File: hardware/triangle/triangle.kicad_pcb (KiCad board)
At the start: 4 copper layers, 100 x 86.6 mm, 71 parts, among them J1 USB_C_Receptacle_USB2.0_16P, J2 USB_C_Receptacle_USB2.0_16P, U2 EA8212HT6R

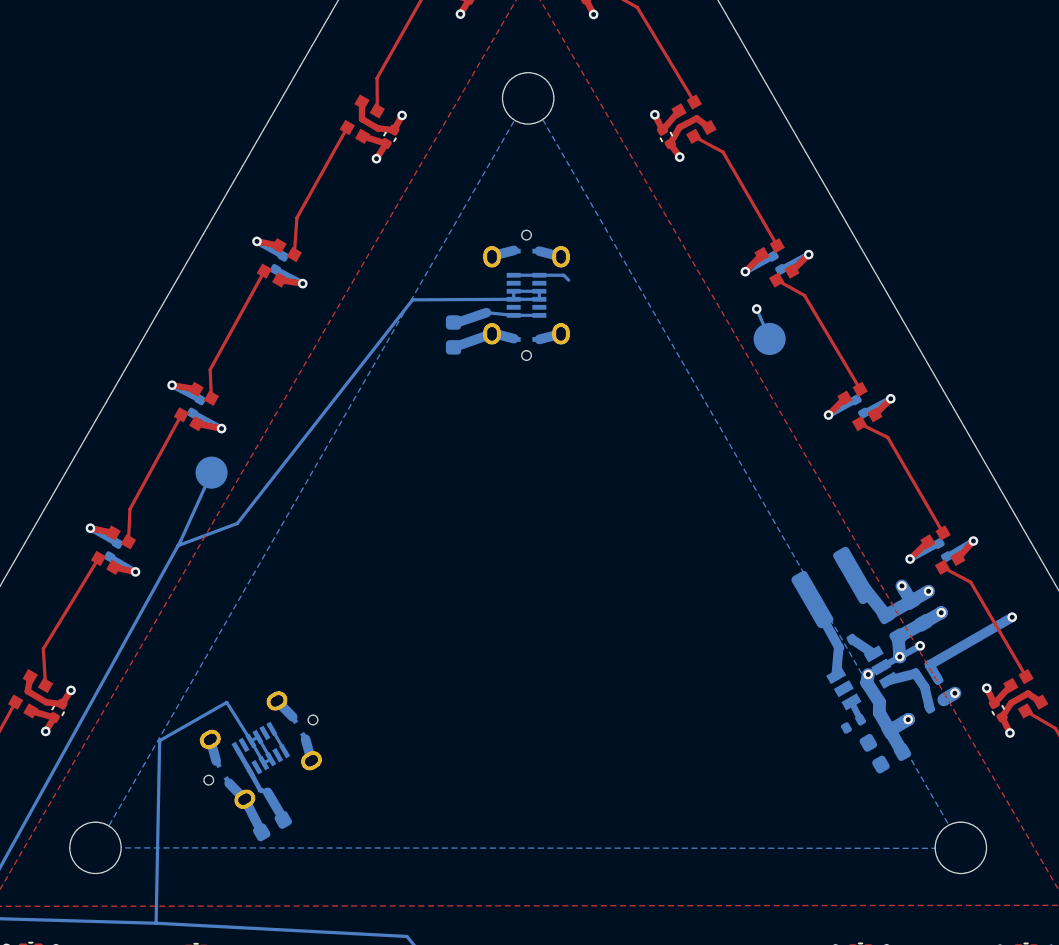
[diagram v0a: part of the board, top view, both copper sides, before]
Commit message: updates to schematic based on feedback
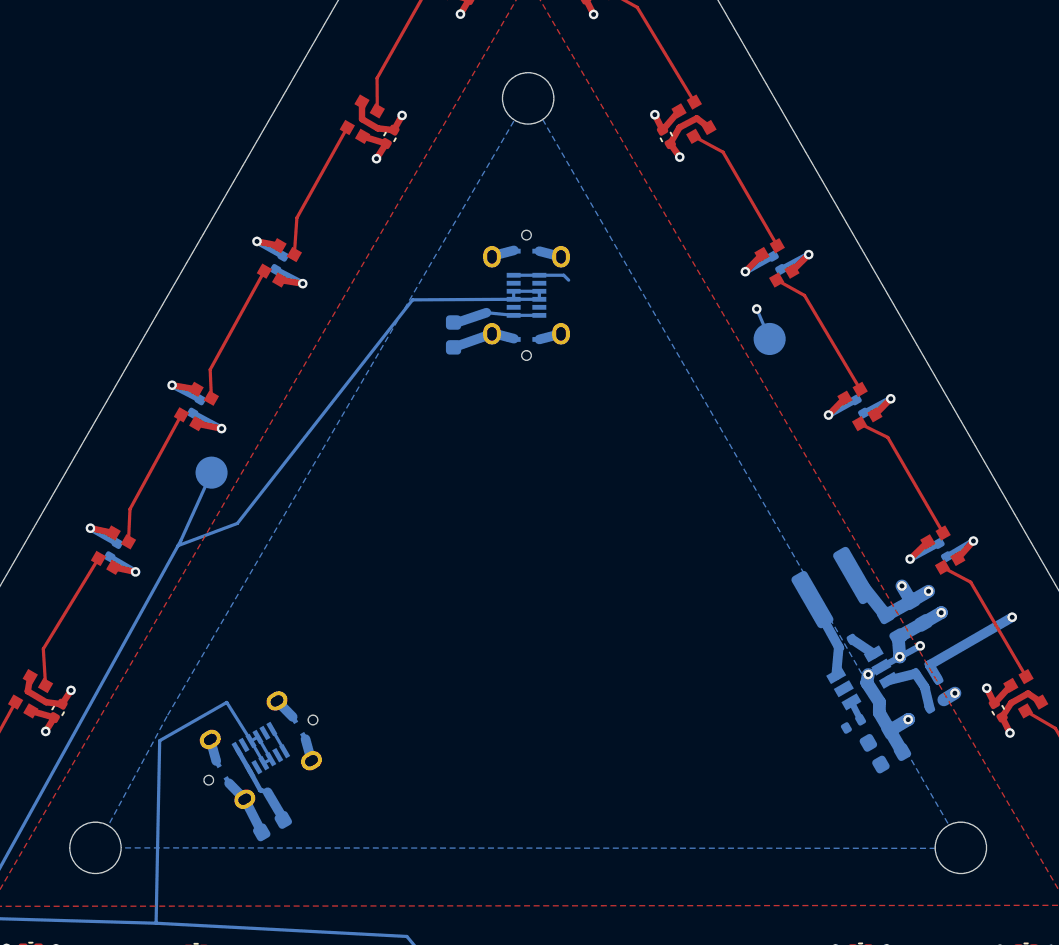
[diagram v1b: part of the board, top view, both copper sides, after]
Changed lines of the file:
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@@
 		)
 		(property "Value" "10µF"
-			(at 0 -1.430001 30)
+			(at -0.000001 -1.430001 30)
 			(layer "B.Fab")
 			(effects
@@
 		(polygon
 			(pts
-				(xy 150.01 89.87) (xy 123.09 136.7) (xy 177.05 136.73) (xy 150.02 89.78)
+				(xy 150.01 89.87) (xy 127.5 128.5) (xy 123.09 136.7) (xy 130.750025 136.704259) (xy 177.05 136.73)
+				(xy 150.02 89.78)
 			)
 		)

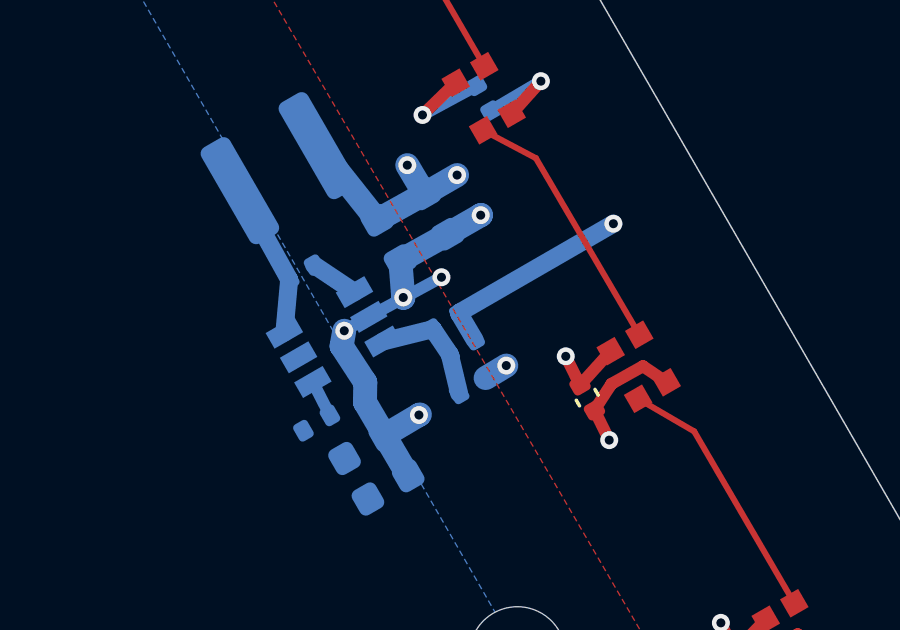
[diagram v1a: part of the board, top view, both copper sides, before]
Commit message: remove unused capacitor from triangle board
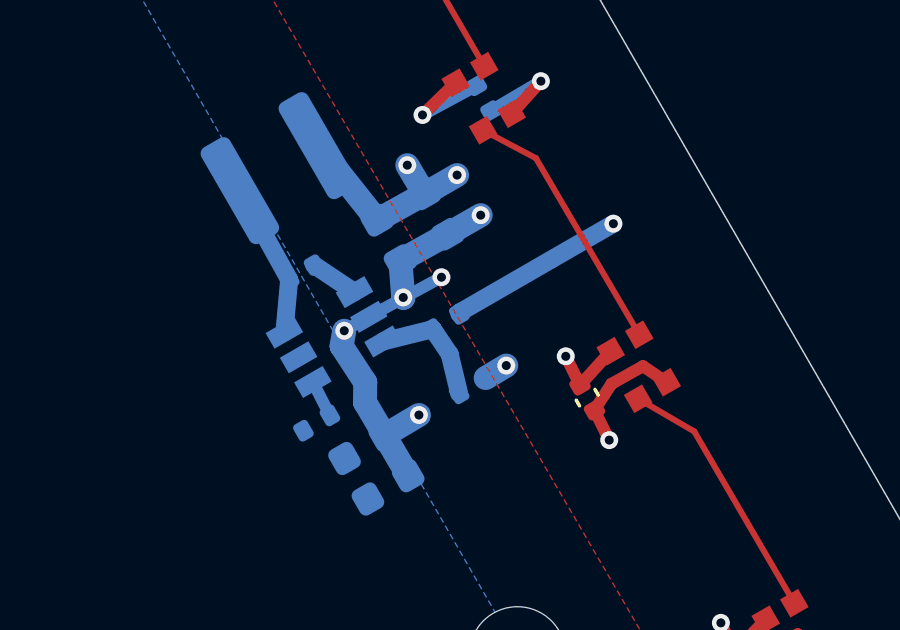
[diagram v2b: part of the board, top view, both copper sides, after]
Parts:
- removed C32: 33nF, Capacitor_SMD:C_0402_1005Metric
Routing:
- net +4V: track 112.4 -> 111.4 mm
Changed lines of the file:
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@@
 		)
 	)
-	(footprint "Capacitor_SMD:C_0402_1005Metric"
-		(layer "B.Cu")
-		(at 175.12 126.44 30)
-		(descr "Capacitor SMD 0402 (1005 Metric), square (rectangular) end terminal, IPC-7351 nominal, (Body size source: IPC-SM-782 page 76, https://www.pcb-3d.com/wordpress/wp-content/uploads/ipc-sm-782a_amendment_1_and_2.pdf)")
-		(tags "capacitor")
-		(property "Reference" "C32"
-			(at 2.606403 0.465577 210)
-			(layer "B.SilkS")
-			(effects
-				(font
-					(size 1 1)
-					(thickness 0.15)
-				)
-				(justify mirror)
-			)
-		)
-		(property "Value" "33nF"
-			(at 0 -1.16 210)
-			(layer "B.Fab")
-			(effects
-				(font
-					(size 1 1)
-					(thickness 0.15)
-				)
-				(justify mirror)
-			)
-		)
-		(property "Datasheet" "https://www.lcsc.com/datasheet/lcsc_datasheet_2304140030_Samsung-Electro-Mechanics-CL05B104KO5NNNC_C1525.pdf"
-			(at 0 0 210)
-			(layer "B.Fab")
-			(hide yes)
-			(effects
-				(font
-					(size 1.27 1.27)
-				)
-				(justify mirror)
-			)
-		)
-		(property "Description" "Unpolarized capacitor"
-			(at 0 0 210)
-			(layer "B.Fab")
-			(hide yes)
-			(effects
-				(font
-					(size 1.27 1.27)
-				)
-				(justify mirror)
-			)
-		)
-		(property "KiLib_Generator" "SMD_2terminal_chip_molded"
-			(at 0 0 210)
-			(layer "B.SilkS")
-			(hide yes)
-			(effects
-				(font
-					(size 1 1)
-					(thickness 0.15)
-				)
-				(justify mirror)
-			)
-		)
-		(property "LCSC Part #" "C507072"
-			(at 0 0 210)
-			(unlocked yes)
-			(layer "B.Fab")
-			(hide yes)
-			(effects
-				(font
-					(size 1 1)
-					(thickness 0.15)
-				)
-				(justify mirror)
-			)
-		)
-		(property ki_fp_filters "C_*")
-		(sheetname "/")
-		(sheetfile "usb_and_power.kicad_sch")
-		(units
-			(unit
-				(name "A")
-				(pins "1" "2")
-			)
-		)
-		(attr smd dnp)
-		(duplicate_pad_numbers_are_jumpers no)
-		(fp_line
-			(start -0.107836 -0.36)
-			(end 0.107836 -0.36)
-			(stroke
-				(width 0.12)
-				(type solid)
-			)
-			(layer "B.SilkS")
-		)
-		(fp_line
-			(start -0.107836 0.36)
-			(end 0.107836 0.36)
-			(stroke
-				(width 0.12)
-				(type solid)
-			)
-			(layer "B.SilkS")
-		)
-		(fp_poly
-			(pts
-				(xy -0.91 -0.46) (xy 0.91 -0.46) (xy 0.91 0.46) (xy -0.91 0.46)
-			)
-			(stroke
-				(width 0.05)
-				(type solid)
-			)
-			(fill no)
-			(layer "B.CrtYd")
-		)
-		(fp_poly
-			(pts
-				(xy -0.5 -0.25) (xy 0.5 -0.25) (xy 0.5 0.25) (xy -0.5 0.25)
-			)
-			(stroke
-				(width 0.1)
-				(type solid)
-			)
-			(fill no)
-			(layer "B.Fab")
-		)
-		(fp_text user "${REFERENCE}"
-			(at 0 0 210)
-			(layer "B.Fab")
-			(effects
-				(font
-					(size 0.25 0.25)
-					(thickness 0.04)
-				)
-				(justify mirror)
-			)
-		)
-		(pad "1" smd roundrect
-			(at -0.48 0 30)
-			(size 0.56 0.62)
-			(layers "B.Cu" "B.Mask" "B.Paste")
-			(roundrect_rratio 0.25)
-			(net "Net-(U2-FBK)")
-			(pintype "passive")
-		)
-		(pad "2" smd roundrect
-			(at 0.48 0 30)
-			(size 0.56 0.62)
-			(layers "B.Cu" "B.Mask" "B.Paste")
-			(roundrect_rratio 0.25)
-			(net "+4V")
-			(pintype "passive")
-		)
-		(embedded_fonts no)
-		(model "${KICAD10_3DMODEL_DIR}/Capacitor_SMD.3dshapes/C_0402_1005Metric.step"
-			(offset
-				(xyz 0 0 0)
-			)
-			(scale
-				(xyz 1 1 1)
-			)
-			(rotate
-				(xyz 0 0 0)
-			)
-		)
-	)
 	(footprint "Capacitor_SMD:C_0603_1608Metric"
 		(layer "B.Cu")
@@
 	)
 	(segment
-		(start 175.02419 125.334923)
-		(end 175.535692 126.2)
-		(width 0.6)
-		(layer "B.Cu")
-		(net "+4V")
-	)
-	(segment
 		(start 172.2825 122.21883)
 		(end 173.8625 121.33883)
@@
 	)
 	(segment
-		(start 173.678602 128.708602)
-		(end 173.71 128.69)
-		(width 0.8)
-		(layer "B.Cu")
-		(net "GND")
-	)
-	(segment
 		(start 172.54117 129.3825)
 		(end 173.678602 128.708602)
@@
 		(layer "B.Cu")
 		(net "GND")
-	)
-	(segment
-		(start 175.737312 122.047312)
-		(end 175.75 122.04)
-		(width 0.8)
-		(layer "B.Cu")
-		(net "GND")

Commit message: script for making brackets, also scoot over components on triangle board
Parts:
- moved C34 9.77 mm to (167.4, 122.9)
- moved R3 9.77 mm to (170.2, 119.5)
- moved U2 9.77 mm to (165.6, 117.9)
- moved C26 9.77 mm to (164.5, 115.7)
- moved C27 9.77 mm to (166.6, 121.5)
- moved C28 9.77 mm to (167.4, 114.7)
- moved C31 9.77 mm to (169.0, 113.8)
- moved L1 9.77 mm to (163.8, 112.2)
- moved R4 9.77 mm to (169.3, 117.4)
- moved R9 9.77 mm to (165.0, 120.7)
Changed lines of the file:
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@@
 	(footprint "Resistor_SMD:R_0402_1005Metric"
 		(layer "B.Cu")
-		(at 174.582517 125.589923 30)
+		(at 169.322517 117.359923 30)
 		(descr "Resistor SMD 0402 (1005 Metric), square (rectangular) end terminal, IPC-7351 nominal, (Body size source: IPC-SM-782 page 72, https://www.pcb-3d.com/wordpress/wp-content/uploads/ipc-sm-782a_amendment_1_and_2.pdf)")
 		(tags "resistor")
@@
 	(footprint "Resistor_SMD:R_0402_1005Metric"
 		(layer "B.Cu")
-		(at 175.46 127.73 30)
+		(at 170.2 119.5 30)
 		(descr "Resistor SMD 0402 (1005 Metric), square (rectangular) end terminal, IPC-7351 nominal, (Body size source: IPC-SM-782 page 72, https://www.pcb-3d.com/wordpress/wp-content/uploads/ipc-sm-782a_amendment_1_and_2.pdf)")
 		(tags "resistor")
@@
 	(footprint "Capacitor_SMD:C_0603_1608Metric"
 		(layer "B.Cu")
-		(at 172.67 122.89 -60)
+		(at 167.41 114.66 -60)
 		(descr "Capacitor SMD 0603 (1608 Metric), square (rectangular) end terminal, IPC-7351 nominal, (Body size source: IPC-SM-782 page 76, https://www.pcb-3d.com/wordpress/wp-content/uploads/ipc-sm-782a_amendment_1_and_2.pdf)")
 		(tags "capacitor")
@@
 	(footprint "Capacitor_SMD:C_0603_1608Metric"
 		(layer "B.Cu")
-		(at 171.87 129.77 30)
+		(at 166.61 121.54 30)
 		(descr "Capacitor SMD 0603 (1608 Metric), square (rectangular) end terminal, IPC-7351 nominal, (Body size source: IPC-SM-782 page 76, https://www.pcb-3d.com/wordpress/wp-content/uploads/ipc-sm-782a_amendment_1_and_2.pdf)")
 		(tags "capacitor")
@@
 	(footprint "Capacitor_SMD:C_0603_1608Metric"
 		(layer "B.Cu")
-		(at 174.25 122.01 -60)
+		(at 168.99 113.78 -60)
 		(descr "Capacitor SMD 0603 (1608 Metric), square (rectangular) end terminal, IPC-7351 nominal, (Body size source: IPC-SM-782 page 76, https://www.pcb-3d.com/wordpress/wp-content/uploads/ipc-sm-782a_amendment_1_and_2.pdf)")
 		(tags "capacitor")
@@
 	(footprint "Resistor_SMD:R_0402_1005Metric"
 		(layer "B.Cu")
-		(at 170.270098 128.976405 -150)
+		(at 165.010098 120.746405 -150)
 		(descr "Resistor SMD 0402 (1005 Metric), square (rectangular) end terminal, IPC-7351 nominal, (Body size source: IPC-SM-782 page 72, https://www.pcb-3d.com/wordpress/wp-content/uploads/ipc-sm-782a_amendment_1_and_2.pdf)")
 		(tags "resistor")
@@
 	(footprint "Capacitor_SMD:C_0603_1608Metric"
 		(layer "B.Cu")
-		(at 172.65 131.12 30)
+		(at 167.39 122.89 30)
 		(descr "Capacitor SMD 0603 (1608 Metric), square (rectangular) end terminal, IPC-7351 nominal, (Body size source: IPC-SM-782 page 76, https://www.pcb-3d.com/wordpress/wp-content/uploads/ipc-sm-782a_amendment_1_and_2.pdf)")
 		(tags "capacitor")
@@
 	(footprint "Capacitor_SMD:C_0402_1005Metric"
 		(layer "B.Cu")
-		(at 169.769118 123.950793 -150)
+		(at 164.509118 115.720793 -150)
 		(descr "Capacitor SMD 0402 (1005 Metric), square (rectangular) end terminal, IPC-7351 nominal, (Body size source: IPC-SM-782 page 76, https://www.pcb-3d.com/wordpress/wp-content/uploads/ipc-sm-782a_amendment_1_and_2.pdf)")
 		(tags "capacitor")
@@
 	(footprint "footprints:SOT-23-6_L2.9-W1.6-P0.95-LS2.8-BR"
 		(layer "B.Cu")
-		(at 170.836901 126.109661 30)
+		(at 165.576901 117.879661 30)
 		(property "Reference" "U2"
 			(at -3.052453 -0.006798 30)
@@
 	(footprint "Inductor_SMD:L_Changjiang_FNR4030S"
 		(layer "B.Cu")
-		(at 169.01 120.48 30)
+		(at 163.75 112.25 30)
 		(descr "Inductor, Changjiang, FNR4030S, 4.0x4.0x3.0mm, (https://datasheet.lcsc.com/lcsc/1806131217_cjiang-Changjiang-Microelectronics-Tech-FNR5040S3R3NT_C167960.pdf)")
 		(tags "wirewound power shielded")
@@
 	)
 	(via
-		(at 180.160029 122.331211)
+		(at 174.900029 114.101211)
 		(size 0.6)
 		(drill 0.3)
@@
 	)
 	(via
-		(at 174.95 120.71)
+		(at 169.69 112.48)
 		(size 0.6)
 		(drill 0.3)
@@
 	)
 	(via
-		(at 173.29 120.38)
+		(at 168.03 112.15)
 		(size 0.6)
 		(drill 0.3)
@@
 	)
 	(segment
-		(start 175.036405 125.289337)
-		(end 180.160029 122.331211)
+		(start 169.776405 117.059337)
+		(end 174.900029 114.101211)
 		(width 0.6)
 		(layer "B.Cu")
@@
 	)
 	(segment
-		(start 170.309038 119.729999)
-		(end 172.2825 122.21883)
+		(start 165.049038 111.499999)
+		(end 167.0225 113.98883)
 		(width 0.8)
 		(layer "B.Cu")
@@
 	)
 	(segment
-		(start 173.8625 121.33883)
-		(end 174.95 120.71)
+		(start 168.6025 113.10883)
+		(end 169.69 112.48)
 		(width 0.8)
 		(layer "B.Cu")
@@
 	)
 	(segment
-		(start 175.02419 125.334923)
-		(end 175.036405 125.289337)
+		(start 169.76419 117.104923)
+		(end 169.776405 117.059337)
 		(width 0.6)
 		(layer "B.Cu")
@@
 	)
 	(segment
-		(start 172.2825 122.21883)
-		(end 173.8625 121.33883)
+		(start 167.0225 113.98883)
+		(end 168.6025 113.10883)
 		(width 0.8)
 		(layer "B.Cu")
@@
 	)
 	(segment
-		(start 173.8625 121.33883)
-		(end 173.29 120.38)
+		(start 168.6025 113.10883)
+		(end 168.03 112.15)
 		(width 0.8)
 		(layer "B.Cu")
@@
 	)
 	(via
-		(at 176.59 127.06)
+		(at 171.33 118.83)
 		(size 0.6)
 		(drill 0.3)
@@
 	)
 	(via
-		(at 173.156315 124.79)
+		(at 167.896315 116.56)
 		(size 0.6)
 		(drill 0.3)
@@
 	)
 	(via
-		(at 175.737312 122.047312)
+		(at 170.477312 113.817312)
 		(size 0.6)
 		(drill 0.3)
@@
 	)
 	(via
-		(at 173.678602 128.708602)
+		(at 168.418602 120.478602)
 		(size 0.6)
 		(drill 0.3)
@@
 	)
 	(via
-		(at 174.429761 124.115333)
+		(at 169.169761 115.885333)
 		(size 0.6)
 		(drill 0.3)
@@
 	)
 	(via
-		(at 171.19 125.9)
+		(at 165.93 117.67)
 		(size 0.6)
 		(drill 0.3)
@@
 	)
 	(segment
-		(start 174.6375 122.68117)
-		(end 175.737312 122.047312)
+		(start 169.3775 114.45117)
+		(end 170.477312 113.817312)
 		(width 0.8)
 		(layer "B.Cu")
@@
 	)
 	(segment
-		(start 173.157742 124.807742)
-		(end 174.429761 124.115333)
+		(start 167.897742 116.577742)
+		(end 169.169761 115.885333)
 		(width 0.4)
 		(layer "B.Cu")
@@
 	)
 	(segment
-		(start 172.006035 125.434661)
-		(end 171.19 125.9)
+		(start 166.746035 117.204661)
+		(end 165.93 117.67)
 		(width 0.4)
 		(layer "B.Cu")
@@
 	)
 	(segment
-		(start 171.89 127.62)
-		(end 171.88 128.28)
+		(start 166.63 119.39)
+		(end 166.62 120.05)
 		(width 0.8)
 		(layer "B.Cu")
@@
 	)
 	(segment
-		(start 173.0575 123.56117)
-		(end 173.156315 124.79)
+		(start 167.7975 115.33117)
+		(end 167.896315 116.56)
 		(width 0.8)
 		(layer "B.Cu")
@@
 	)
 	(segment
-		(start 172.54117 129.3825)
-		(end 173.678602 128.708602)
+		(start 167.28117 121.1525)
+		(end 168.418602 120.478602)
 		(width 0.8)
 		(layer "B.Cu")
@@
 	)
 	(segment
-		(start 171.19 125.9)
-		(end 171.1 126.41)
+		(start 165.93 117.67)
+		(end 165.84 118.18)
 		(width 0.8)
 		(layer "B.Cu")
@@
 	)
 	(segment
-		(start 172.006035 125.434661)
-		(end 173.157742 124.807742)
+		(start 166.746035 117.204661)
+		(end 167.897742 116.577742)
 		(width 0.4)
 		(layer "B.Cu")
@@
 	)
 	(segment
-		(start 171.1 126.41)
-		(end 171.89 127.62)
+		(start 165.84 118.18)
+		(end 166.63 119.39)
 		(width 0.8)
 		(layer "B.Cu")
@@
 	)
 	(segment
-		(start 175.901673 127.475)
-		(end 176.59 127.06)
+		(start 170.641673 119.245)
+		(end 171.33 118.83)
 		(width 0.8)
 		(layer "B.Cu")
@@
 	)
 	(segment
-		(start 173.156315 124.79)
-		(end 173.157742 124.807742)
+		(start 167.896315 116.56)
+		(end 167.897742 116.577742)
 		(width 0.8)
 		(layer "B.Cu")
@@
 	)
 	(segment
-		(start 173.0575 123.56117)
-		(end 174.6375 122.68117)
+		(start 167.7975 115.33117)
+		(end 169.3775 114.45117)
 		(width 0.8)
 		(layer "B.Cu")
@@
 	)
 	(segment
-		(start 171.88 128.28)
-		(end 173.32117 130.7325)
+		(start 166.62 120.05)
+		(end 168.06117 122.5025)
 		(width 0.8)
 		(layer "B.Cu")
@@
 	)
 	(segment
-		(start 174.704308 126.68)
-		(end 175.018327 127.985)
+		(start 169.444308 118.45)
+		(end 169.758327 119.755)
 		(width 0.6)
 		(layer "B.Cu")
@@
 	)
 	(segment
-		(start 174.140844 125.844923)
-		(end 174.704308 126.68)
+		(start 168.880844 117.614923)
+		(end 169.444308 118.45)
 		(width 0.6)
 		(layer "B.Cu")
@@
 	)
 	(segment
-		(start 172.481035 126.257385)
-		(end 174.140844 125.844923)
+		(start 167.221035 118.027385)
+		(end 168.880844 117.614923)
 		(width 0.6)
 		(layer "B.Cu")
@@
 	)
 	(segment
-		(start 170.142766 127.607385)
-		(end 170.711771 128.721405)
+		(start 164.882766 119.377385)
+		(end 165.451771 120.491405)
 		(width 0.4)
 		(layer "B.Cu")
@@
 	)
 	(segment
-		(start 170.18481 123.710793)
-		(end 171.531035 124.611936)
+		(start 164.92481 115.480793)
+		(end 166.271035 116.381936)
 		(width 0.6)
 		(layer "B.Cu")
@@
 	)
 	(segment
-		(start 169.353426 124.190793)
-		(end 167.710962 121.230001)
+		(start 164.093426 115.960793)
+		(end 162.450962 113.000001)
 		(width 0.6)
 		(layer "B.Cu")
@@
 	)
 	(segment
-		(start 169.353426 124.190793)
-		(end 169.192766 125.961936)
+		(start 164.093426 115.960793)
+		(end 163.932766 117.731936)
 		(width 0.6)
 		(layer "B.Cu")
